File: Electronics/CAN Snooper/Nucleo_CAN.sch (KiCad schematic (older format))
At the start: 35 parts, among them J1 CAN_In, J2 CAN_Out, SW1 Reset, T1 12V Iso Test, T10 CAN L Test, T11 CAN Output GND Test, T2 5V Iso Test, T3 9V Test, T4 3.3V Test, T5 CAN PwrSense Test, T6 CAN Tx Test, T7 CAN Rx Test, T8 CAN Input GND Test, T9 CAN H Test, U1 PDS1-S12-S9-M, U2 MCP1702T-5002E/CB, U3 Nucleo_L432KC, U4 ADM3054

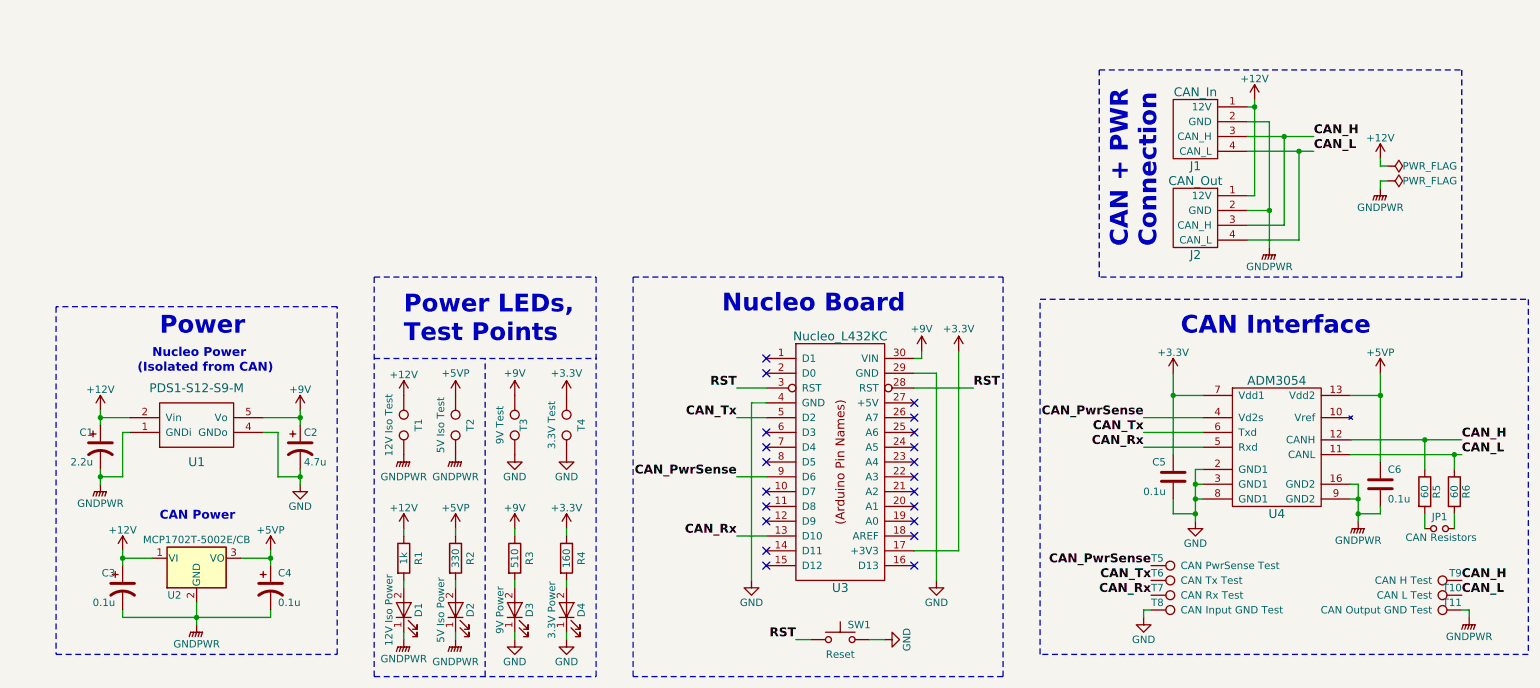
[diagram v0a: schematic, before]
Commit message: CAN Snooper: Schematic: Page size is US Letter; rearranged blocks.
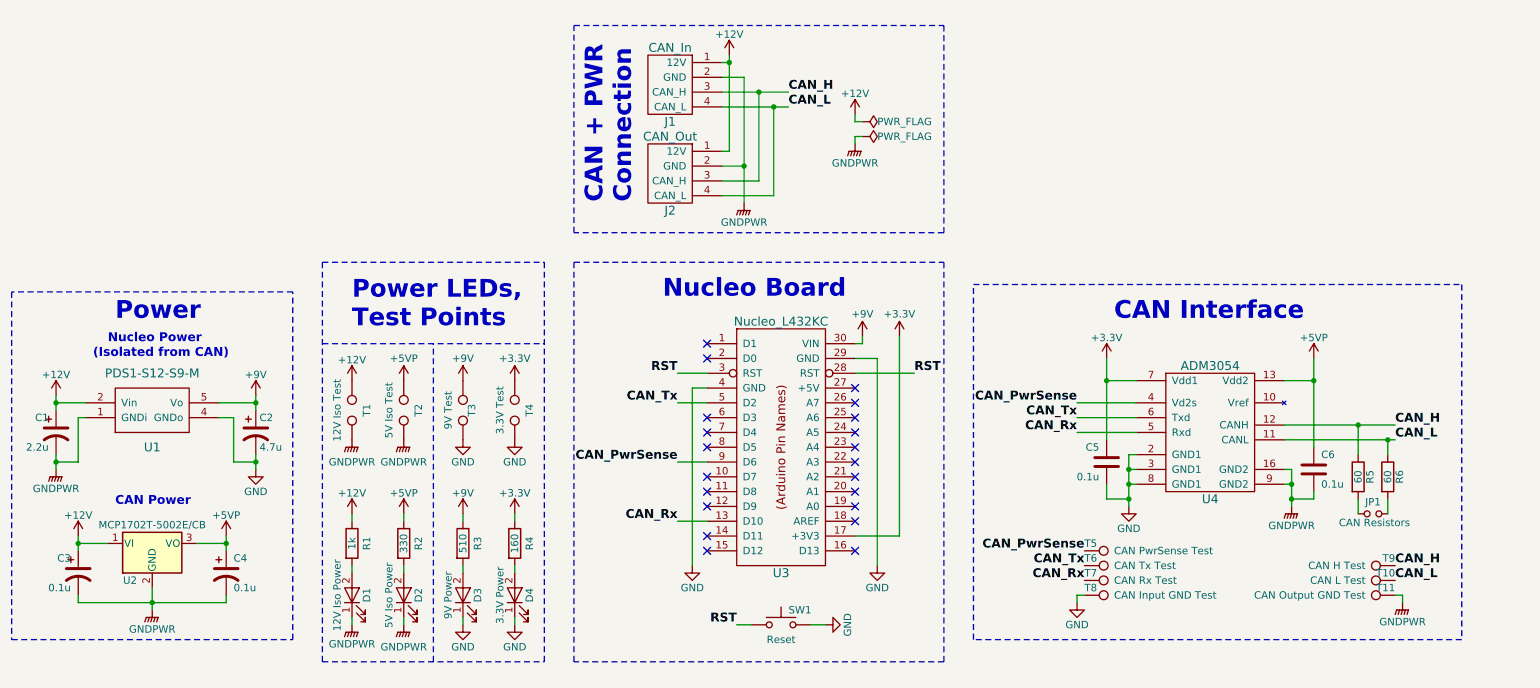
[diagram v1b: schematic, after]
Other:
- moved on the sheet: C1, C2, C3, C4, C5, C6, D1, D2, D3, D4, J1, J2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
